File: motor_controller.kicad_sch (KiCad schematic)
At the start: 33 parts, among them IC3 DRV8301DCAR

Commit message: Routing done
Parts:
- removed C27: 100nF, Capacitor_SMD:C_0402_1005Metric, symbol Device:C
- removed C30: 68uF, Capacitor_Tantalum_SMD:CP_EIA-7361-438_AVX-U_Pad2.18x3.30mm_HandSolder, symbol Device:C_Polarized_Small
- removed D4: D, Diode_SMD:D_0805_2012Metric, symbol Device:D
- removed L2: 22uH, Inductor_SMD:L_Bourns-SRN4018, symbol Device:L
- removed R11, R12: 120R, Resistor_SMD:R_0805_2012Metric, symbol Device:R
- removed R4: 18K, Resistor_SMD:R_0402_1005Metric, symbol Device:R
- removed R5: 3.3K, Resistor_SMD:R_0402_1005Metric, symbol Device:R
- added R3: 10K, Resistor_SMD:R_0402_1005Metric, symbol Device:R
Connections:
- net GND: now also R3.1
- net SN1: now also C25.1, IC3.33 (SN1)
- net SN2: now also C28.1, IC3.31 (SN2)
- net at IC3.50 (PH_1): no longer IC3.51 (PH_2)
- net at IC3.55 (EN_BUCK): now also R3.2
- no-connect marks 3 -> 5

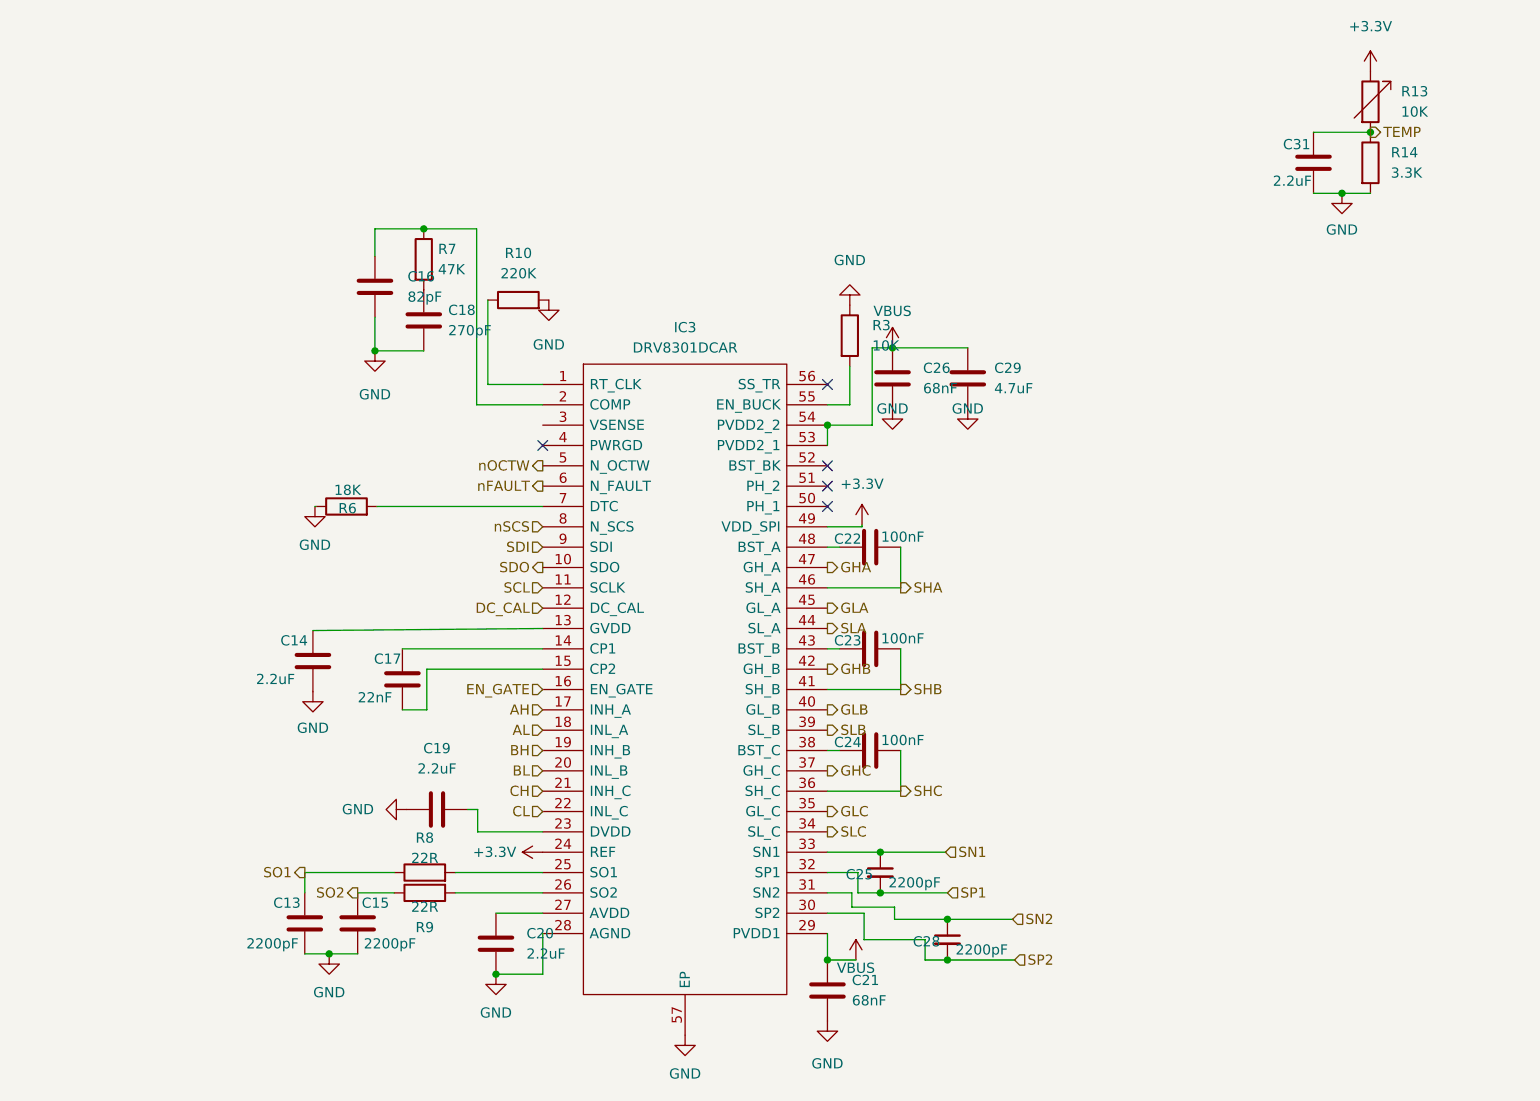
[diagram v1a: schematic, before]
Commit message: Using DRV8353 with built in current sense
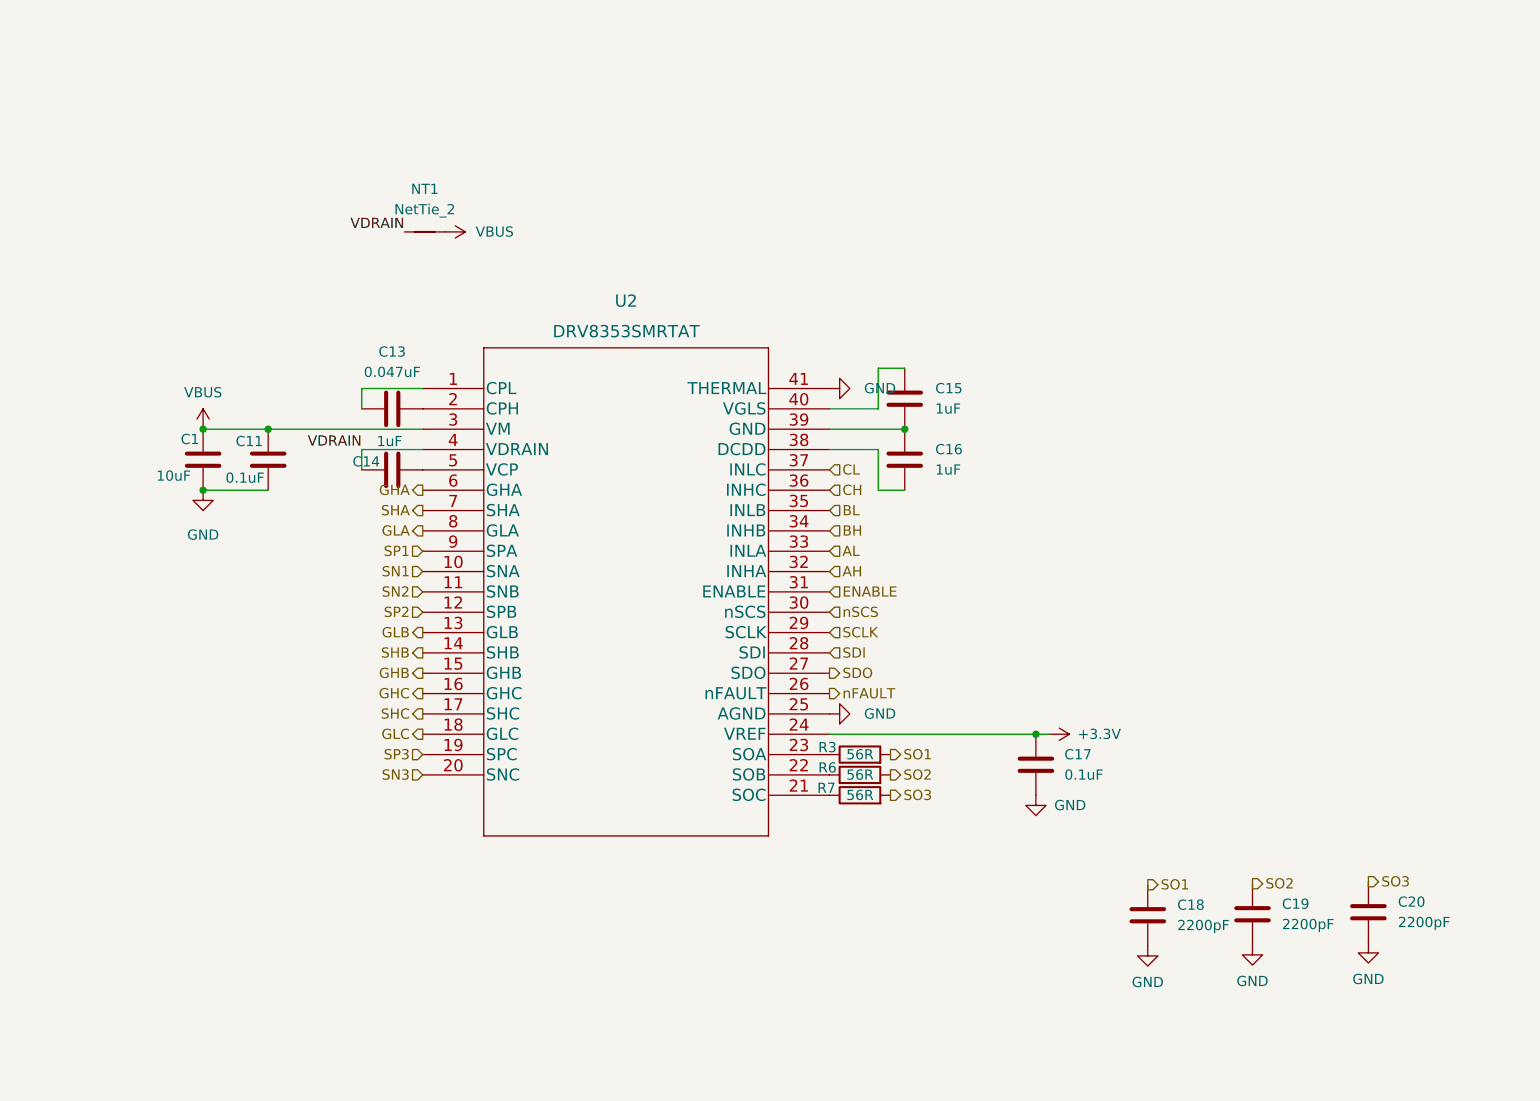
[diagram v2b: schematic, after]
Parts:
- removed C21, C26: 68nF, Capacitor_SMD:C_0402_1005Metric, symbol Device:C
- removed C22, C23, C24: 100nF, Capacitor_SMD:C_0402_1005Metric, symbol Device:C
- removed C25, C28: 2200pF, Capacitor_SMD:C_0402_1005Metric, symbol Device:C_Small
- removed C29: 4.7uF, Capacitor_SMD:C_0402_1005Metric, symbol Device:C
- removed C31: 2.2uF, Capacitor_SMD:C_0402_1005Metric, symbol Device:C
- removed IC3: DRV8301DCAR, DRV8301:SOP50P810X120-57N, symbol DRV8301DCAR:DRV8301DCAR
- removed R10: 220K, Resistor_SMD:R_0402_1005Metric, symbol Device:R
- removed R13: 10K, Resistor_SMD:R_0402_1005Metric, symbol Device:R_Variable
- removed R14: 3.3K, Resistor_SMD:R_0402_1005Metric, symbol Device:R
- removed R8, R9: 22R, Resistor_SMD:R_0402_1005Metric, symbol Device:R
- added C1: 10uF, Capacitor_SMD:C_1210_3225Metric, symbol Device:C
- added C11: 0.1uF, Capacitor_SMD:C_0402_1005Metric, symbol Device:C
- added NT1: NetTie_2, NetTie:NetTie-2_SMD_Pad0.5mm, symbol Device:NetTie_2
- added U2: DRV8353SMRTAT, DRV8353M:DRV8353SMRTAT, symbol DRV8353SMRTAT:DRV8353SMRTAT
- C13: value 2200pF -> 0.047uF
- C14: value 2.2uF -> 1uF
- C15: value 2200pF -> 1uF
- C16: value 82pF -> 1uF
- C17: value 22nF -> 0.1uF
- C18: value 270pF -> 2200pF
- C19, C20: value 2.2uF -> 2200pF
- R3: value 10K -> 56R
- R6: value 18K -> 56R
- R7: value 47K -> 56R
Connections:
- net +3.3V: now also C17.1, U2.24 (VREF)
- net AH: now also U2.32 (INHA)
- net AL: now also U2.33 (INLA)
- net BH: now also U2.34 (INHB)
- net BL: now also U2.35 (INLB)
- net CH: now also U2.36 (INHC)
- net CL: now also U2.37 (INLC)
- net GHA: now also U2.6 (GHA)
- net GHB: now also U2.15 (GHB)
- net GHC: now also U2.16 (GHC)
- net GLA: now also U2.8 (GLA)
- net GLB: now also U2.13 (GLB)
- net GLC: now also U2.18 (GLC)
- net GND: now also C17.2, C19.2, C1.2, C11.2, U2.25 (AGND), U2.41 (THERMAL); no longer C13.2, C14.2, C15.2, C16.2, C19.1, R3.1, R6.1
- net SDI: now also U2.28 (SDI)
- net SDO: now also U2.27 (SDO)
- net SHA: now also U2.7 (SHA)
- net SHB: now also U2.14 (SHB)
- net SHC: now also U2.17 (SHC)
- net SN1: now also U2.10 (SNA)
- net SN2: now also U2.11 (SNB)
- net SO1: now also C18.1, R3.2; no longer C13.1
- net SO2: now also C19.1, R6.2; no longer C15.1
- net SP1: now also U2.9 (SPA)
- net SP2: now also U2.12 (SPB)
- net VBUS: now also C1.1, C11.1, NT1.2, U2.3 (VM)
- net nFAULT: now also U2.26 (nFAULT)
- net nSCS: now also U2.30 (nSCS)
- net at R7.1: now also U2.21 (SOC); no longer C16.1
- net SO3: now reaches R7.2
- net SO3: now also C20.1; no longer C18.1
- net VDRAIN: now reaches C14.1
- net VDRAIN: now also NT1.1, U2.4 (VDRAIN)
- new net: C13.1, U2.1 (CPL)
- new net: C13.2, U2.2 (CPH)
- new net: R6.1, U2.22 (SOB)
- new net: R3.1, U2.23 (SOA)
- new net: C16.2, U2.38 (DCDD)
- new net: C15.2, C16.1, U2.39 (GND)
- new net: C15.1, U2.40 (VGLS)
- new net: C14.2, U2.5 (VCP)
- new net ENABLE: U2.31 (ENABLE)
- new net SCLK: U2.29 (SCLK)
- new net SN3: U2.20 (SNC)
- new net SP3: U2.19 (SPC)
- no-connect marks 5 -> 0

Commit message: init routing done
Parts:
- removed U2: DRV8353SMRTAT, DRV8353M:DRV8353SMRTAT, symbol DRV8353SMRTAT:DRV8353SMRTAT
- added C24: 22uF, Capacitor_SMD:C_0805_2012Metric, symbol Device:C
- added C8: 1uF, Capacitor_SMD:C_0402_1005Metric, symbol Device:C
- added D4: D, Diode_SMD:D_0603_1608Metric, symbol Device:D
- added IC2: DRV8323RHRGZR, DRV8323:QFN50P700X700X100-49N-D, symbol DRV8323RHRGZR:DRV8323RHRGZR
- added L1: 15uH, Inductor_SMD:L_0805_2012Metric, symbol Device:L
- added R15, R16, R21, R23: 75K, Resistor_SMD:R_0402_1005Metric, symbol Device:R
- added R17: 28K, Resistor_SMD:R_0402_1005Metric, symbol Device:R
- added R18: 8.45K, Resistor_SMD:R_0402_1005Metric, symbol Device:R
- added R20: 47K, Resistor_SMD:R_0402_1005Metric, symbol Device:R
- added R24: 10K, Resistor_SMD:R_0402_1005Metric, symbol Device:R
- added R25: 330, Resistor_SMD:R_0402_1005Metric, symbol Device:R
- C1: value 10uF -> 4.7uF; footprint Capacitor_SMD:C_1210_3225Metric -> Capacitor_SMD:C_0805_2012Metric
- C15: value 1uF -> 2.2uF
- C16: value 1uF -> 0.1uF
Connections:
- net +3.3V: now also C24.1, D4.1 (K), IC2.26 (VREF), R15.1, R17.1, R21.1, R24.1
- net AH: now also IC2.37 (INHA)
- net AL: now also IC2.38 (INLA)
- net BH: now also IC2.39 (INHB)
- net BL: now also IC2.40 (INLB)
- net CH: now also IC2.41 (INHC)
- net CL: now also IC2.42 (INLC)
- net ENABLE: now also IC2.33 (ENABLE)
- net GHA: now also IC2.8 (GHA)
- net GHB: now also IC2.17 (GHB)
- net GHC: now also IC2.18 (GHC)
- net GLA: now also IC2.10 (GLA)
- net GLB: now also IC2.15 (GLB)
- net GLC: now also IC2.20 (GLC)
- net GND: now also C15.2, C24.2, IC2.2 (PGND), IC2.43 (BGND), IC2.49 (THERMAL_PAD), R16.2, R18.2, R20.2, R23.2, R25.2; no longer C17.2, C18.2, C19.2, C20.2
- net SHA: now also IC2.9 (SHA)
- net SHB: now also IC2.16 (SHB)
- net SHC: now also IC2.19 (SHC)
- net SN1: now also IC2.12 (SNA)
- net SN2: now also IC2.13 (SNB)
- net SN3: now also IC2.22 (SNC)
- net SP1: now also IC2.11 (SPA)
- net SP2: now also IC2.14 (SPB)
- net SP3: now also IC2.21 (SPC)
- net VBUS: now also C15.1, IC2.47 (VIN), IC2.48 (NSHDN), IC2.5 (VCP)
- net VDRAIN: now also IC2.6 (VM)
- net nFAULT: now also IC2.28 (NFAULT), R24.2, R25.1
- net at C13.1: now also IC2.3 (CPL)
- net at C13.2: now also IC2.4 (CPH)
- net at R7.1: now also IC2.23 (SOC)
- net at R6.1: now also IC2.24 (SOB)
- net at R3.1: now also IC2.25 (SOA)
- net at C16.2: now also IC2.44 (CB)
- net at C16.1: now also IC2.45 (SW), L1.1; no longer C15.2
- net at C14.2: now also IC2.7 (VDRAIN)
- new net: C8.1, IC2.36 (DVDD)
- new net: D4.2 (A), L1.2
- new net CAL: IC2.34 (CAL)
- new net FB: IC2.1 (FB), R17.2, R18.1
- new net GAIN: IC2.32 (GAIN), R20.1
- new net GNDD: C17.2, C18.2, C19.2, C20.2, C8.2, IC2.27 (DGND), IC2.35 (AGND)
- new net IDRIVE: IC2.30 (IDRIVE), R21.2, R23.1
- new net MODE: IC2.29 (MODE)
- new net VDS: IC2.31 (VDS), R15.2, R16.1
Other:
- moved on the sheet: C1, C11, C13, C14, C17, NT1, R3, R6, R7
